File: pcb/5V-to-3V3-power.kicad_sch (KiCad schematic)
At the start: 12 parts, among them J1 USB_C_Receptacle_USB2.0, U1 AMS1117-3.3

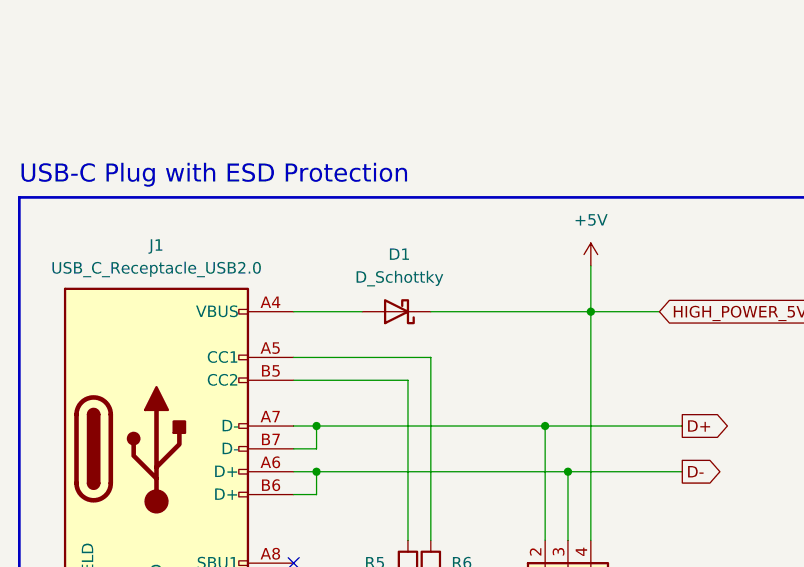
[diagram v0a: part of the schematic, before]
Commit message: ADD 3D Models for all footprints, export new PCB Image and remove D1 for R8 with 0R (Jumper R)
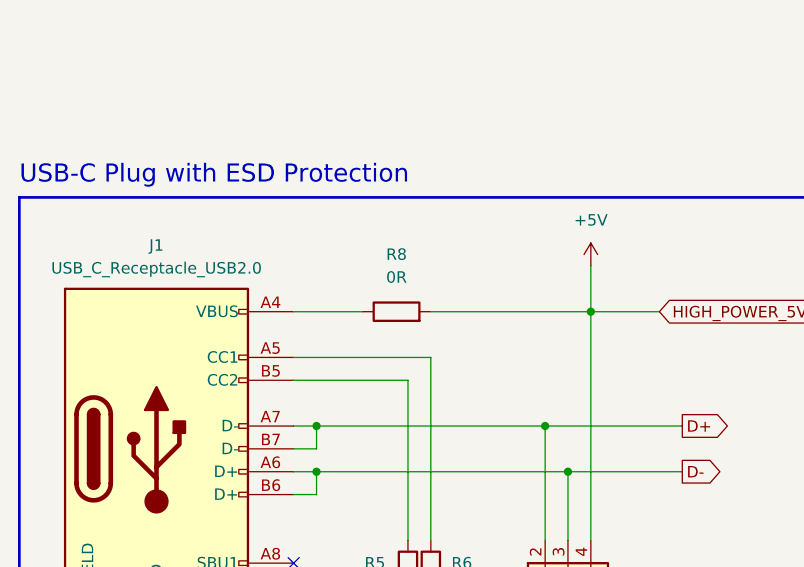
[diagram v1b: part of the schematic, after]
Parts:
- removed D1: D_Schottky, Diode_SMD:D_0805_2012Metric, symbol Device:D_Schottky
- added R8: 0R, Resistor_SMD:R_0805_2012Metric_Pad1.20x1.40mm_HandSolder, symbol Device:R
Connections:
- net +5V: now also R8.2
- net at J1.A4 (VBUS), J1.A9 (VBUS), J1.B4 (VBUS)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: now also R8.1
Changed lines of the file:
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@@
     (pin "1")
+  )
+  (symbol (lib_id "Device:R") (at 95.25 81.28 90) (unit 1)
+    (in_bom yes) (on_board yes) (fields_autoplaced)
+    (property "Reference" "R8" (id 0) (at 95.25 74.93 90))
+    (property "Value" "0R" (id 1) (at 95.25 77.47 90))
+    (property "Footprint" "Resistor_SMD:R_0805_2012Metric_Pad1.20x1.40mm_HandSolder" (id 2) (at 95.25 83.058 90)
+      (effects (font (size 1.27 1.27)) hide)
+    )
+    (property "Datasheet" "~" (id 3) (at 95.25 81.28 0)
+      (effects (font (size 1.27 1.27)) hide)
+    )
+    (pin "1")
+    (pin "2")
   )
   (symbol (lib_id "power:+3.3V") (at 223.52 58.42 0) (unit 1)
@@
       (effects (font (size 1.27 1.27)) hide)
     )
-    (pin "1")
-    (pin "2")
-  )
-  (symbol (lib_id "Device:D_Schottky") (at 95.25 81.28 180) (unit 1)
-    (in_bom yes) (on_board yes) (fields_autoplaced)
-    (property "Reference" "D1" (id 0) (at 95.5675 74.93 0))
-    (property "Value" "D_Schottky" (id 1) (at 95.5675 77.47 0))
-    (property "Footprint" "Diode_SMD:D_0805_2012Metric" (id 2) (at 95.25 81.28 0)
-      (effects (font (size 1.27 1.27)) hide)
-    )
-    (property "Datasheet" "~" (id 3) (at 95.25 81.28 0)
-      (effects (font (size 1.27 1.27)) hide)
-    )

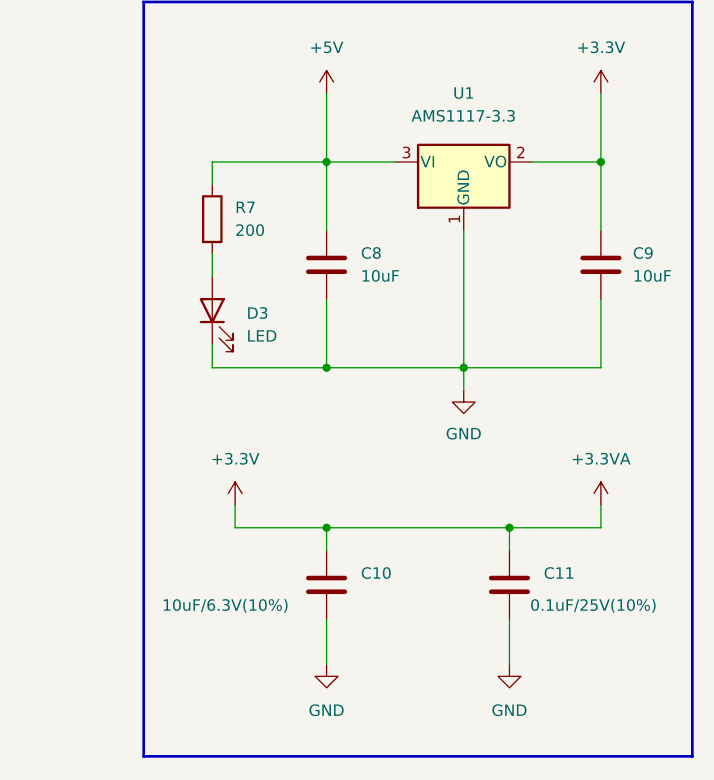
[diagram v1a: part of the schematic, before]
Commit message: ADD new picture, and propper GND plane on top layer
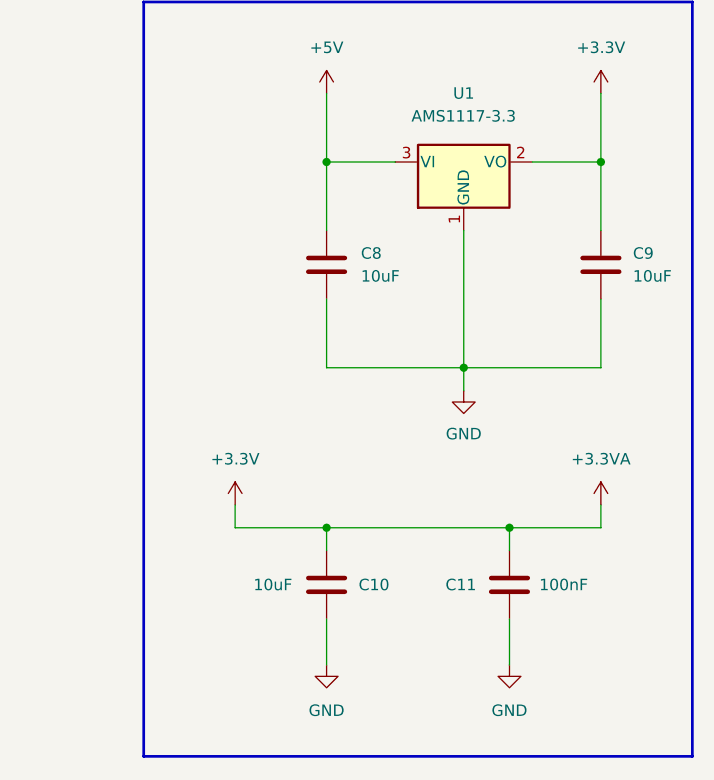
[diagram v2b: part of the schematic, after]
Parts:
- removed D3: LED, LED_SMD:LED_0402_1005Metric, symbol Device:LED
- removed R7: 200, Resistor_SMD:R_0402_1005Metric, symbol Device:R
- C10: value 10uF/6.3V(10%) -> 10uF
- C11: value 0.1uF/25V(10%) -> 100nF
- C8: footprint Capacitor_SMD:C_0603_1608Metric_Pad1.08x0.95mm_HandSolder -> Capacitor_SMD:C_0603_1608Metric
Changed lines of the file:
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@@
   (junction (at 86.36 99.06) (diameter 0) (color 0 0 0 0)
-  )
-  (junction (at 193.04 88.9) (diameter 0) (color 0 0 0 0)
   )
   (junction (at 208.28 88.9) (diameter 0) (color 0 0 0 0)
@@
     (stroke (width 0) (type default) (color 0 0 0 0))
   )
-  (wire (pts (xy 180.34 66.04) (xy 193.04 66.04))
-    (stroke (width 0) (type default) (color 0 0 0 0))
-  )
-  (wire (pts (xy 180.34 76.2) (xy 180.34 78.74))
-    (stroke (width 0) (type default) (color 0 0 0 0))
-  )
   (wire (pts (xy 83.82 96.52) (xy 86.36 96.52))
     (stroke (width 0) (type default) (color 0 0 0 0))
@@
     (stroke (width 0) (type default) (color 0 0 0 0))
   )
-  (wire (pts (xy 180.34 88.9) (xy 193.04 88.9))
-    (stroke (width 0) (type default) (color 0 0 0 0))
-  )
   (wire (pts (xy 213.36 109.22) (xy 213.36 106.68))
     (stroke (width 0) (type default) (color 0 0 0 0))
@@
     (stroke (width 0) (type default) (color 0 0 0 0))
   )
-  (wire (pts (xy 180.34 88.9) (xy 180.34 86.36))
-    (stroke (width 0) (type default) (color 0 0 0 0))
-  )
   (polyline (pts (xy 53.34 68.58) (xy 53.34 134.62))
     (stroke (width 0.3) (type default) (color 25 28 255 1))
@@
   )
   (wire (pts (xy 116.84 76.2) (xy 116.84 81.28))
-    (stroke (width 0) (type default) (color 0 0 0 0))
-  )
-  (wire (pts (xy 180.34 68.58) (xy 180.34 66.04))
     (stroke (width 0) (type default) (color 0 0 0 0))
   )
@@
     (pin "1")
   )
-  (symbol (lib_id "Device:R") (at 180.34 72.39 0) (unit 1)
-    (in_bom yes) (on_board yes) (fields_autoplaced)
-    (property "Reference" "R7" (id 0) (at 182.88 71.1199 0)
-      (effects (font (size 1.27 1.27)) (justify left))
-    )
-    (property "Value" "200" (id 1) (at 182.88 73.6599 0)
-      (effects (font (size 1.27 1.27)) (justify left))
-    )
-    (property "Footprint" "Resistor_SMD:R_0402_1005Metric" (id 2) (at 178.562 72.39 90)
-      (effects (font (size 1.27 1.27)) hide)
-    )
-    (property "Datasheet" "~" (id 3) (at 180.34 72.39 0)
-      (effects (font (size 1.27 1.27)) hide)
-    )
-    (pin "1")
-    (pin "2")
-  )
   (symbol (lib_id "power:GND") (at 208.28 91.44 0) (unit 1)
     (in_bom yes) (on_board yes) (fields_autoplaced)
@@
       (effects (font (size 1.27 1.27)) (justify left))
     )
-    (property "Footprint" "Capacitor_SMD:C_0603_1608Metric_Pad1.08x0.95mm_HandSolder" (id 2) (at 194.0052 81.28 0)
+    (property "Footprint" "Capacitor_SMD:C_0603_1608Metric" (id 2) (at 194.0052 81.28 0)
       (effects (font (size 1.27 1.27)) hide)
     )
@@
   (symbol (lib_id "Device:C") (at 213.36 113.03 0) (unit 1)
     (in_bom yes) (on_board yes)
-    (property "Reference" "C11" (id 0) (at 217.17 111.7599 0)
-      (effects (font (size 1.27 1.27)) (justify left))
-    )
-    (property "Value" "0.1uF/25V(10%)" (id 1) (at 215.646 115.316 0)
+    (property "Reference" "C11" (id 0) (at 206.248 113.03 0)
+      (effects (font (size 1.27 1.27)) (justify left))
+    )
+    (property "Value" "100nF" (id 1) (at 216.662 113.03 0)
       (effects (font (size 1.27 1.27)) (justify left))
     )
@@
     )
     (property "Datasheet" "~" (id 3) (at 213.36 113.03 0)
-      (effects (font (size 1.27 1.27)) hide)
-    )
-    (pin "1")
-    (pin "2")
-  )
-  (symbol (lib_id "Device:LED") (at 180.34 82.55 90) (unit 1)
-    (in_bom yes) (on_board yes) (fields_autoplaced)
-    (property "Reference" "D3" (id 0) (at 184.15 82.8674 90)
-      (effects (font (size 1.27 1.27)) (justify right))
-    )
-    (property "Value" "LED" (id 1) (at 184.15 85.4074 90)
-      (effects (font (size 1.27 1.27)) (justify right))
-    )
-    (property "Footprint" "LED_SMD:LED_0402_1005Metric" (id 2) (at 180.34 82.55 0)
-      (effects (font (size 1.27 1.27)) hide)
-    )
-    (property "Datasheet" "~" (id 3) (at 180.34 82.55 0)
       (effects (font (size 1.27 1.27)) hide)
     )
@@
   (symbol (lib_id "Device:C") (at 193.04 113.03 0) (unit 1)
     (in_bom yes) (on_board yes)
-    (property "Reference" "C10" (id 0) (at 196.85 111.7599 0)
-      (effects (font (size 1.27 1.27)) (justify left))
-    )
-    (property "Value" "10uF/6.3V(10%)" (id 1) (at 174.752 115.316 0)
-      (effects (font (size 1.27 1.27)) (justify left))
-    )
+    (property "Reference" "C10" (id 0) (at 196.596 113.03 0)
+      (effects (font (size 1.27 1.27)) (justify left))
+    )
+    (property "Value" "10uF" (id 1) (at 184.912 113.03 0)
+      (effects (font (size 1.27 1.27)) (justify left))
+    )

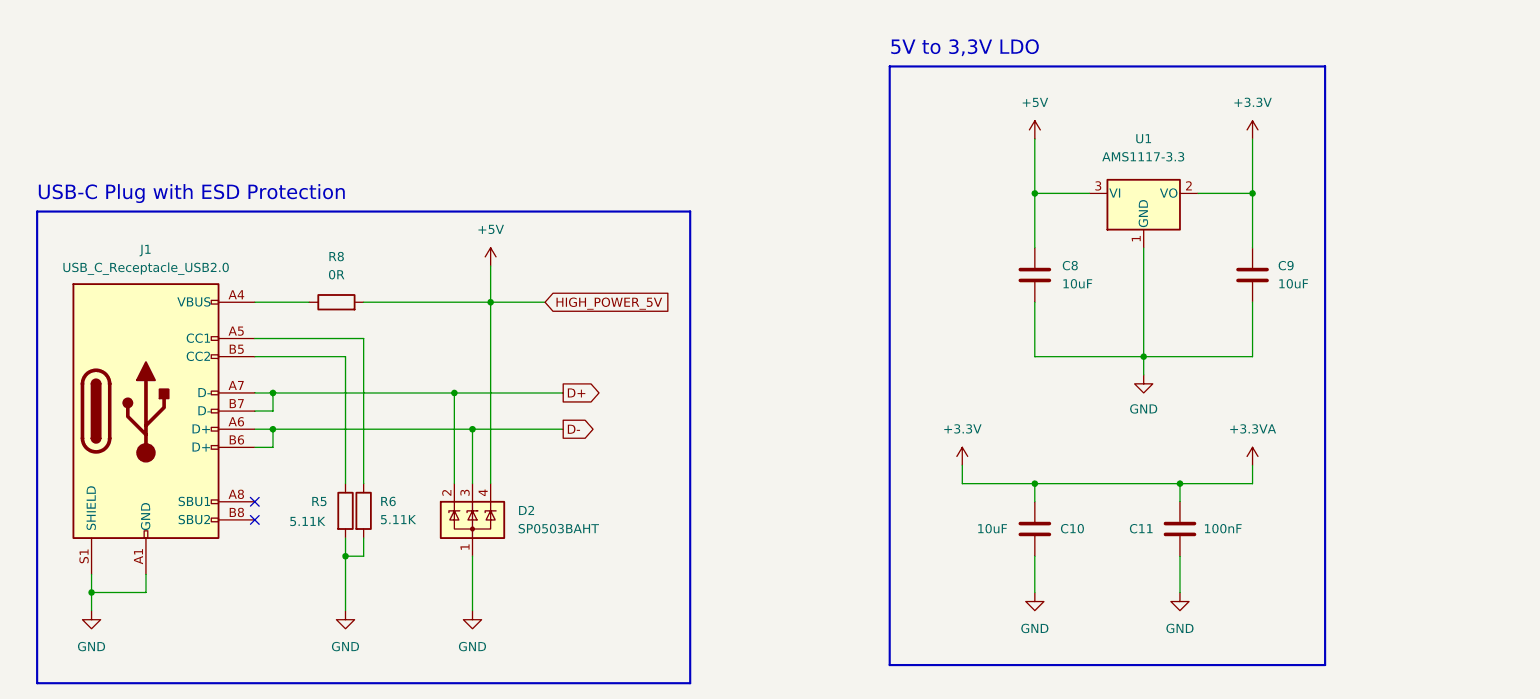
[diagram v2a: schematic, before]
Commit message: REF PCB Layout, Switch to new USB-C Receptable
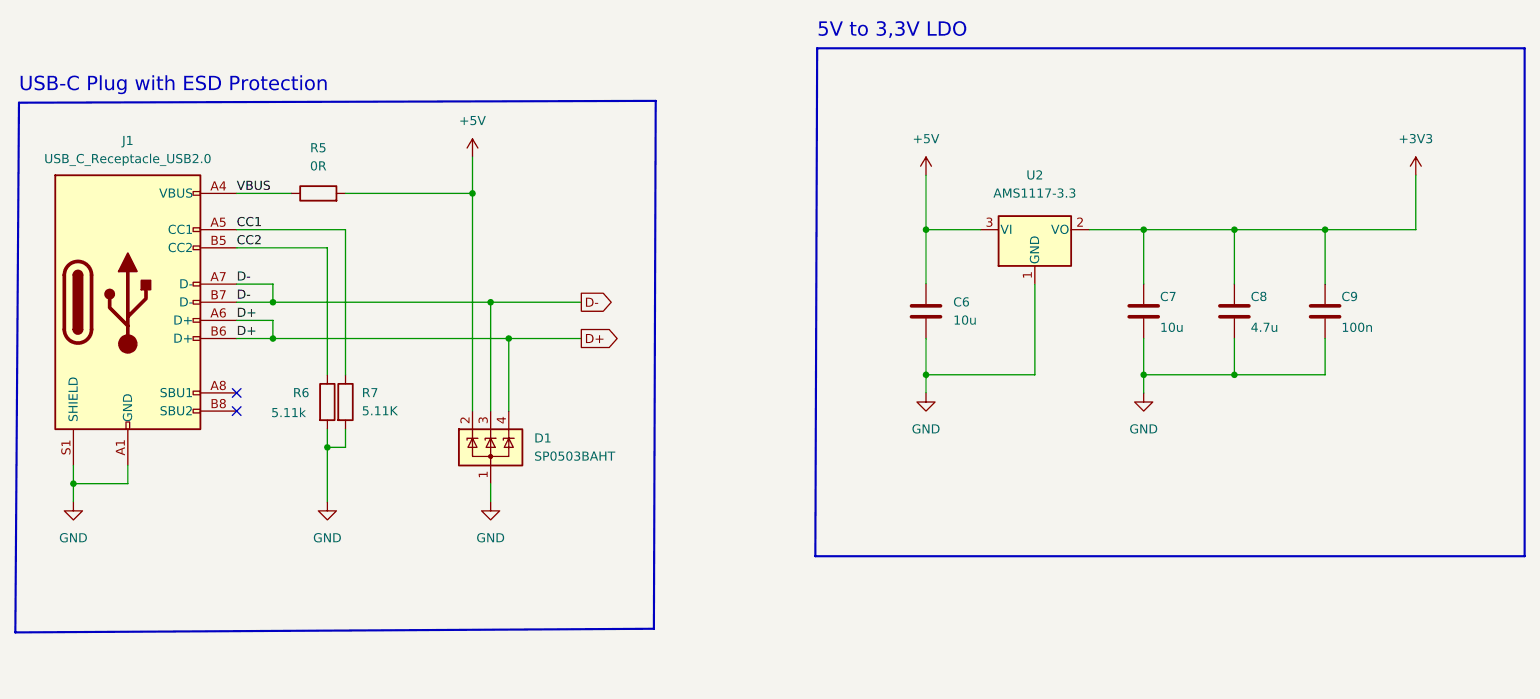
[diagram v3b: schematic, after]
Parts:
- removed C10: 10uF, Capacitor_SMD:C_0603_1608Metric, symbol Device:C
- removed C11: 100nF, Capacitor_SMD:C_0603_1608Metric, symbol Device:C
- removed D2: SP0503BAHT, Package_TO_SOT_SMD:SOT-143, symbol Power_Protection:SP0503BAHT
- removed R8: 0R, Resistor_SMD:R_0805_2012Metric_Pad1.20x1.40mm_HandSolder, symbol Device:R
- removed U1: AMS1117-3.3, Package_TO_SOT_SMD:SOT-223-3_TabPin2, symbol Regulator_Linear:AMS1117-3.3
- added C6: 10u, Capacitor_SMD:C_0603_1608Metric, symbol Device:C
- added C7: 10u, Capacitor_SMD:C_0402_1005Metric, symbol Device:C
- added D1: SP0503BAHT, Package_TO_SOT_SMD:SOT-143, symbol Power_Protection:SP0503BAHT
- added R7: 5.11K, Resistor_SMD:R_0402_1005Metric, symbol Device:R
- added U2: AMS1117-3.3, Package_TO_SOT_SMD:SOT-223-3_TabPin2, symbol Regulator_Linear:AMS1117-3.3
- C8: value 10uF -> 4.7u; footprint Capacitor_SMD:C_0603_1608Metric -> Capacitor_SMD:C_0402_1005Metric
- C9: value 10uF -> 100n; footprint Capacitor_SMD:C_0603_1608Metric -> Capacitor_SMD:C_0402_1005Metric
- J1: footprint Connector_USB:USB_C_Receptacle_HRO_TYPE-C-31-M-12 -> Connector_USB:USB_C_Receptacle_JAE_DX07S016JA1R1500
- R5: value 5.11K -> 0R; footprint Resistor_SMD:R_0603_1608Metric -> Resistor_SMD:R_0805_2012Metric_Pad1.20x1.40mm_HandSolder
- R6: value 5.11K -> 5.11k; footprint Resistor_SMD:R_0603_1608Metric -> Resistor_SMD:R_0402_1005Metric
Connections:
- net +5V: now also R5.2, C6.1, D1.2 (K), U2.3 (VI); no longer C8.1
- net D+: now also J1.A6 (D+), J1.B6 (D+), D1.4 (K); no longer J1.A7 (D-), J1.B7 (D-)
- net D-: now also J1.A7 (D-), J1.B7 (D-), D1.3 (K); no longer J1.A6 (D+), J1.B6 (D+)
- net GND: now also C6.2, C7.2, D1.1 (A), R7.2, U2.1 (GND); no longer R5.2
- net VBUS: now reaches J1.A4 (VBUS), J1.A9 (VBUS), J1.B4 (VBUS), J1.B9 (VBUS)
- net VBUS: now also R5.1
- net CC2: now reaches J1.B5 (CC2)
- net CC2: now also R6.1; no longer R5.1
- net CC1: now reaches J1.A5 (CC1)
- net CC1: now also R7.1; no longer R6.1
- net +3.3VA renamed +3V3
- net +3V3: now also C8.1, C7.1, U2.2 (VO)
